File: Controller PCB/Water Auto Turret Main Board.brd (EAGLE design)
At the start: 82 x 95 mm, 39 parts, among them IC1 DRV8806PWP, IC2 L7805ACV, IC3 PIC12F683-I_P, IC4 SN74LVC2G08DCTR, J1 78171-0004, J10 47053-1000, J2 7691, J3 7691, J4 47053-1000, J5 47053-1000, J6 47053-1000, J7 47053-1000, J8 47053-1000, J9 47053-1000, K1 G5RL-K1A-E, Q1 BC33716BU, Q2 BC33716BU

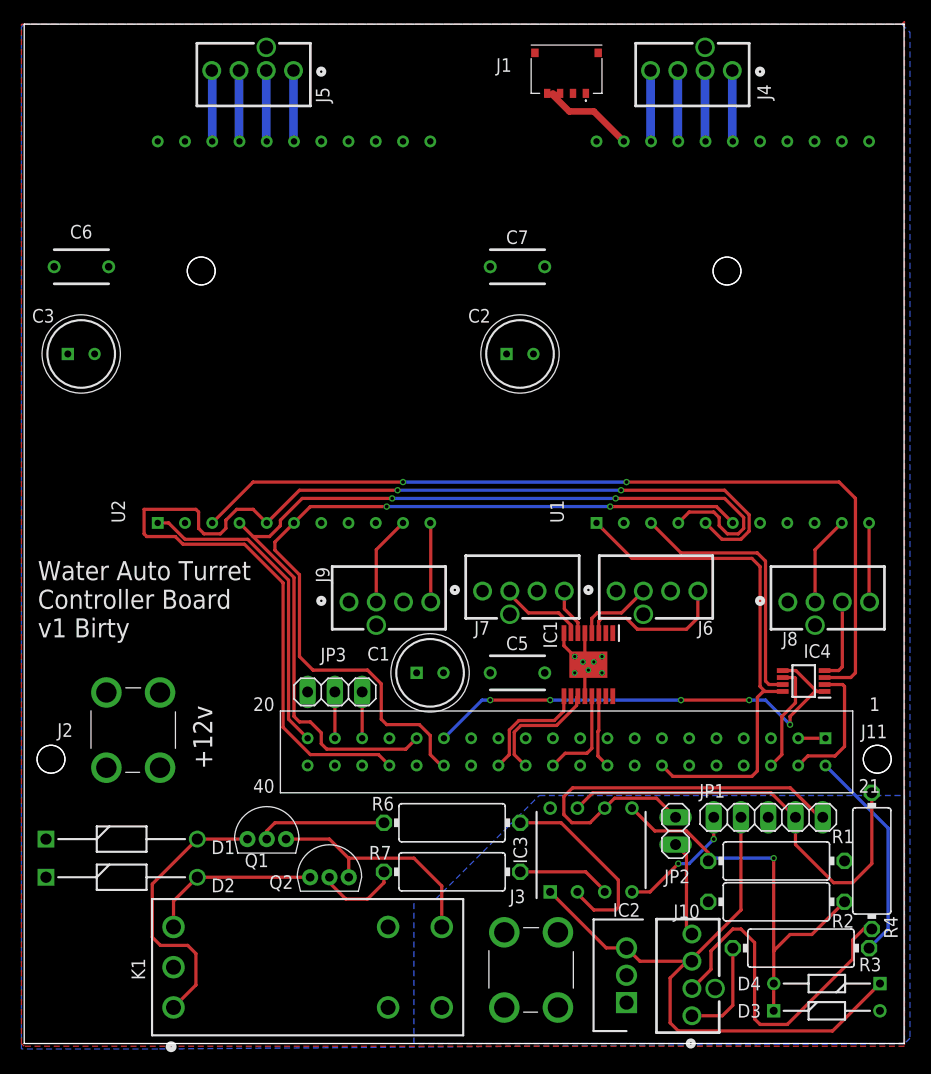
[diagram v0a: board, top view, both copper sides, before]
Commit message: Rev2 PCB
Fixes issues found on Rev1 PCB
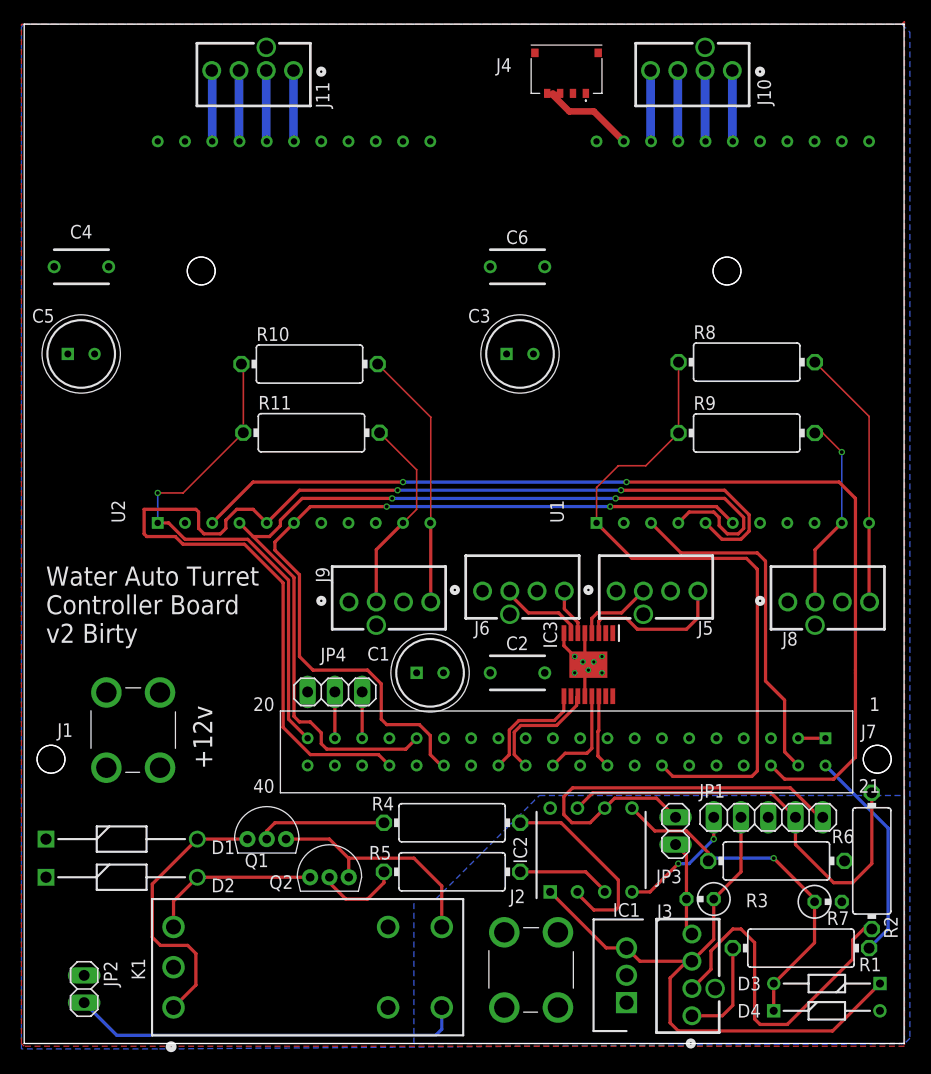
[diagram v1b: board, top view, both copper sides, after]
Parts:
- removed C7: C322C104K1R5TA, SamacSys_Parts:C322C104K1R5TA
- removed IC4: SN74LVC2G08DCTR, SamacSys_Parts:SOP65P400X130-8N
- added C4: C322C104K1R5TA, SamacSys_Parts:C322C104K1R5TA
- added JP4: (no value), pinhead:1X03
- added R10, R11, R8, R9: 8k, resistor:V234/12
- added R5: 1k37, resistor:V234/12
- C2: value 16SEPC100M+TSS -> C322C104K1R5TA; device SamacSys_Parts:CAPPRD250W45D630H600 -> SamacSys_Parts:C322C104K1R5TA
- C5: value C322C104K1R5TA -> 16SEPC100M+TSS; device SamacSys_Parts:C322C104K1R5TA -> SamacSys_Parts:CAPPRD250W45D630H600
- IC1: value DRV8806PWP -> L7805ACV; device SamacSys_Parts:SOP65P640X120-17N -> SamacSys_Parts:TO255P460X1020X2008-3P
- IC2: value L7805ACV -> PIC12F683-I_P; device SamacSys_Parts:TO255P460X1020X2008-3P -> SamacSys_Parts:DIP781W56P254L950H533Q8N
- IC3: value PIC12F683-I_P -> DRV8806PWP; device SamacSys_Parts:DIP781W56P254L950H533Q8N -> SamacSys_Parts:SOP65P640X120-17N
- J1: value 78171-0004 -> 7691; device SamacSys_Parts:781710004 -> SamacSys_Parts-old:7691
- J11: value (none) -> 47053-1000; device VIM3GPIO:VIM3GPIO -> SamacSys_Parts-old:47053-1000
- J3: value 7691 -> 47053-1000; device SamacSys_Parts-old:7691 -> SamacSys_Parts-old:47053-1000
- J4: value 47053-1000 -> 78171-0004; device SamacSys_Parts-old:47053-1000 -> SamacSys_Parts:781710004
- J7: value 47053-1000 -> (none); device SamacSys_Parts-old:47053-1000 -> VIM3GPIO:VIM3GPIO
- JP2: value (none) -> Fan Header
- JP3: device pinhead:1X03 -> pinhead:1X02
- R1: value 8k -> 1k
- R2: value 3k6 -> 1k
- R3: value 1k -> 8k; device resistor:V234/12 -> resistor:0309V
- R4: value 1k -> 1k37
- R6: value (none) -> 8k
- R7: value (none) -> 3k6; device resistor:V234/12 -> resistor:0309V
- moved J10 92.2 mm to (67.6, 93.2), turned to 180 degrees
- moved J11 80.6 mm to (26.7, 93.2), turned to 180 degrees
- moved J1 73.3 mm to (10.2, 29.2), turned to 0 degrees
- moved J5 60.0 mm to (53.6, 39.6), turned to 0 degrees
- moved JP2 57.1 mm to (5.59, 5.08), turned to 270 degrees
- moved C5 51.4 mm to (4.06, 64.3)
- moved J2 43.3 mm to (47.2, 6.86)
- moved C3 40.9 mm to (45.0, 64.3)
- moved C6 40.6 mm to (46.0, 72.4)
- moved R4 39.3 mm to (39.9, 20.6), turned to 0 degrees
- moved J7 35.3 mm to (74.7, 28.4)
- moved R7 35.2 mm to (74.9, 13.2)
- moved JP3 34.3 mm to (60.7, 19.8), turned to 90 degrees
- moved IC1 31.7 mm to (56.1, 3.81), turned to 90 degrees
- moved R6 30.4 mm to (70.1, 17.0), turned to 180 degrees
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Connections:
- removed net N$34: IC4.7, U1.3
- removed net N$41: IC4.8, J11.P$27, U1.1
- removed net N$46: J11.P$20, U2.1
- net +12V: now also C4.1, IC3.1, IC3.2, J1.3, J1.4, J4.1, J4.2, J5.1, J5.3, JP2.1, R6.1; no longer C7.1, IC1.2, IC2.1, J2.1, J2.2, J2.3, J2.4, J7.1, J7.3, R1.1
- net +5V: now also D3.1, IC1.3, IC2.1, J3.3, R3.1; no longer D4.1, IC2.3, IC3.1, J10.3
- net 5V: now also J7.P$1, J7.P$2; no longer J11.P$1, J11.P$2
- net GND: now also D4.2, IC1.2, IC2.8, J2.1, J2.2, J2.3, J2.4, JP2.2, R7.2; no longer D3.2, IC2.2, IC3.8, J3.1, J3.2, J3.3, J3.4, R2.2
- net N$1: now also IC3.4, J5.2; no longer IC1.4, J6.2
- net N$10: now also R4.1; no longer R6.1
- net N$11: now also IC2.7, R2.2; no longer IC3.7, R4.2
- net N$12: now also IC2.6, JP3.2; no longer IC3.6, JP2.2
- net N$13: now also R5.1; no longer R7.1
- net N$14: now also IC2.3, R5.2; no longer IC3.3, R7.2
- net N$15: now also IC2.2, R4.2; no longer IC3.2, R6.2
- net N$16: now also D3.2, D4.1, IC2.5, R6.2, R7.1; no longer D3.1, D4.2, IC3.5, R1.2, R2.1
- net N$17: now also J3.4, JP3.1, R3.2; no longer J10.4, JP2.1
- net N$18: now also J7.P$35; no longer J11.P$35
- net N$19: now also J7.P$37; no longer J11.P$37
- net N$2: now also IC3.3, J5.4; no longer IC1.3, J6.4
- net N$20: now also J7.P$16; no longer J11.P$16
- net N$21: now also J10.4; no longer J4.4
- net N$22: now also J10.3; no longer J4.3
- net N$23: now also J10.1; no longer J4.1
- net N$24: now also J10.2; no longer J4.2
- net N$25: now also J11.4; no longer J5.4
- net N$26: now also J11.2; no longer J5.2
- net N$27: now also J11.1; no longer J5.1
- net N$28: now also J11.3; no longer J5.3
- net N$29: now also R9.2
- net N$3: now also IC3.6, J6.4; no longer IC1.6, J7.4
- net N$30: now also R8.2
- net N$31: now also R11.2
- net N$32: now also R10.2
- net N$33: now also J7.P$20, R10.1, R11.1, U2.1; no longer IC4.1, IC4.5, J11.P$15
- net N$35: now also IC3.14, J7.P$29; no longer IC1.14, J11.P$29
- net N$36: now also IC3.13, J7.P$31; no longer IC1.13, J11.P$31
- net N$37: now also IC3.11, J7.P$32; no longer IC1.11, J11.P$32
- net N$38: now also IC3.9, J7.P$33; no longer IC1.9, J11.P$33
- net N$39: now also J7.P$18, JP4.3; no longer J11.P$18, JP3.3
- net N$4: now also IC3.7, J6.2; no longer IC1.7, J7.2
- net N$40: now also J7.P$19, JP4.2; no longer J11.P$19, JP3.2
- net N$42: now also J7.P$27, R8.1, R9.1, U1.1; no longer IC4.3, U2.3
- net N$44: now also J7.P$22, U1.3; no longer IC4.2, J11.P$22
- net N$45: now also J7.P$23, U2.3; no longer IC4.6, J11.P$23
- net N$5: now also J3.1, R1.2; no longer J10.1, R3.2
- net N$8: now also J3.2, R2.1; no longer J10.2, R4.1
- net N$9: now also IC2.4; no longer IC3.4
- net VSS: now also C4.2, IC3.12, IC3.17, IC3.5, IC3.8, J4.3, J4.4, J7.P$14, J7.P$17, J7.P$21, J7.P$24, J7.P$28, J7.P$34, J7.P$40, J7.P$5, J7.P$9, JP4.1, R1.1; no longer C7.2, IC1.12, IC1.17, IC1.5, IC1.8, IC4.4, J1.3, J1.4, J11.P$14, J11.P$17, J11.P$21, J11.P$24, J11.P$28, J11.P$34, J11.P$40, J11.P$5, J11.P$9, JP3.1, R3.1
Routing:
- net N$45: track 10.3 -> 95.5 mm, vias 0 -> 2
- net N$41: track 47.7 -> 0.00 mm
- net GND: track 21.9 -> 58.8 mm
- net N$46: track 29.9 -> 0.00 mm
- net N$34: track 25.1 -> 0.00 mm
- net N$44: track 12.6 -> 32.5 mm
- net N$30: track 7.39 -> 24.5 mm
- net N$32: track 7.39 -> 24.3 mm
- net N$42: track 81.5 -> 64.7 mm, vias 2 -> 0
- net N$31: track 8.40 -> 18.8 mm
- net N$29: track 8.40 -> 18.3 mm, vias 0 -> 1
- net VSS: track 47.1 -> 39.2 mm
- net N$16: track 38.5 -> 33.2 mm
- net N$33: track 44.3 -> 49.4 mm, vias 5 -> 1
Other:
- board text added: "Water Auto Turret Controller Board v2 Birty"
- board text removed: "Water Auto Turret Controller Board v1 Birty"
